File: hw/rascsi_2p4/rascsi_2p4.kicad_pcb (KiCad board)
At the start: 2 copper layers, 65 x 56 mm, 71 parts, among them J1 Raspberry_Pi_2_3, J10 Conn_01x04_Male, J2 DNP, J20 171826-4, J3 Conn_02x25_Odd_Even, J4 I2C Pinout, J5 DNP, J6 CONNFLY DB-25, J7 DNP, J8 USB_B_Micro, J9 Conn_02x25_Odd_Even, U1 SN74LS641-1DW, U2 SN74LS641-1DW, U3 SN74LS641-1DW, U4 SN74LS641-1DW, U5 UCC5606PWPTR, U6 UCC5606PWPTR, X1 Mac, X3 Mac, X7 Pi, X8 Pi

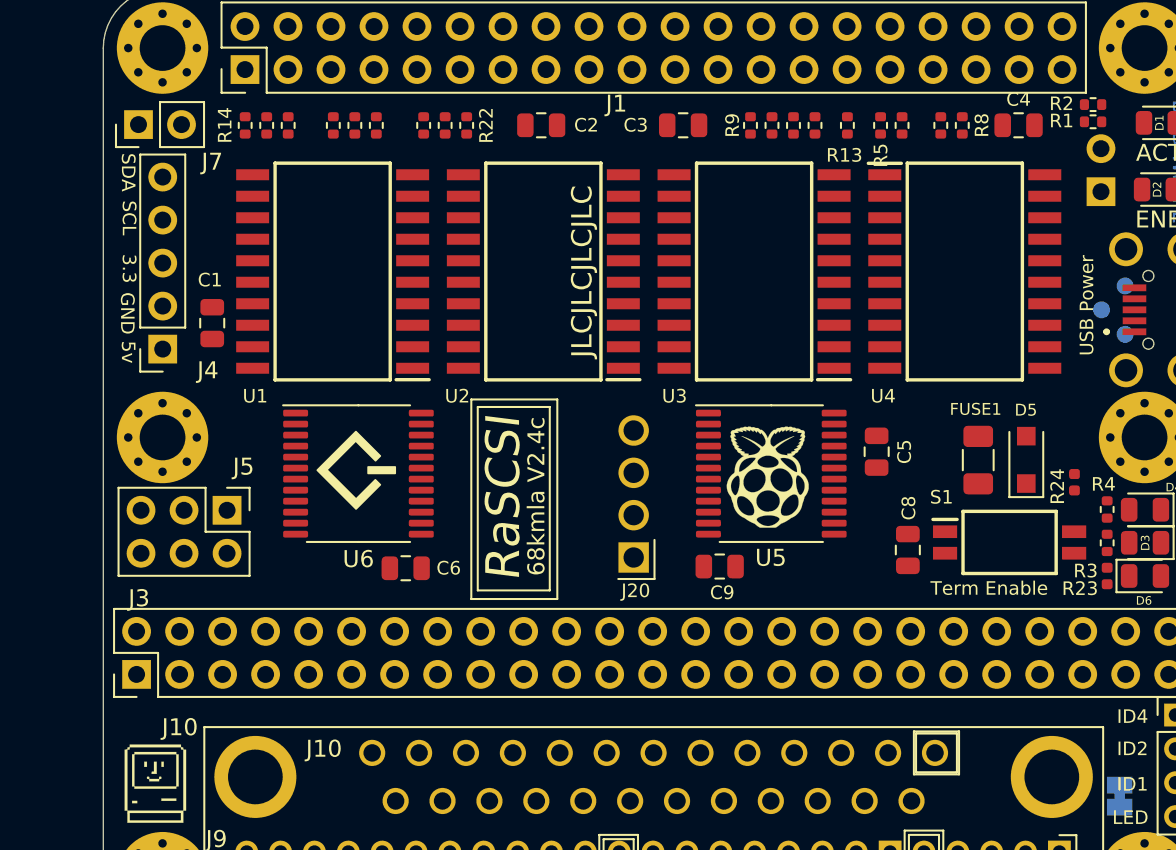
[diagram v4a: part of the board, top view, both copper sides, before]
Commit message: routed with 99 vias but not imported
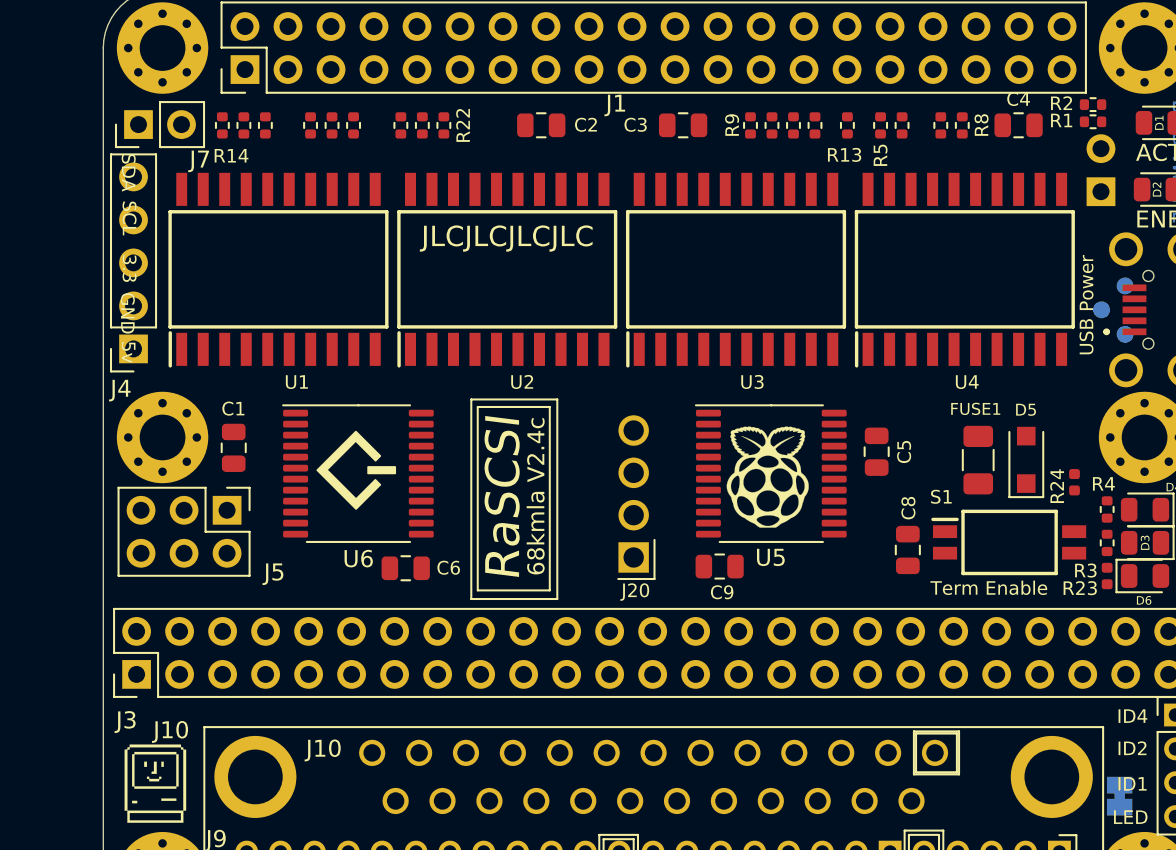
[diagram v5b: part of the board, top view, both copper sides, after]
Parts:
- moved C1 7.47 mm to (182.2, 69.6), turned to 270 degrees
- moved U1 3.20 mm to (184.8, 59.1), turned to 90 degrees
- moved U2 2.14 mm to (198.4, 59.1), turned to 90 degrees
- moved J4 1.72 mm to (176.3, 63.8)
- moved R15 1.35 mm to (182.8, 50.6)
- moved R18 1.35 mm to (188.0, 50.6)
- moved R19 1.35 mm to (189.3, 50.6)
- moved R21 1.35 mm to (193.3, 50.6)
- moved R22 1.35 mm to (194.6, 50.6)
- moved R14 1.35 mm to (181.5, 50.6)
- moved R16 1.35 mm to (184.1, 50.6)
- moved R17 1.35 mm to (186.7, 50.6)
- moved R20 1.35 mm to (192.1, 50.6)
- moved U3 1.07 mm to (211.9, 59.1), turned to 90 degrees
- moved U4 0.13 mm to (225.4, 59.1), turned to 90 degrees
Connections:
- U6 pad 1: C-D7 -> C-D5
- U6 pad 3: C-D5 -> C-D7

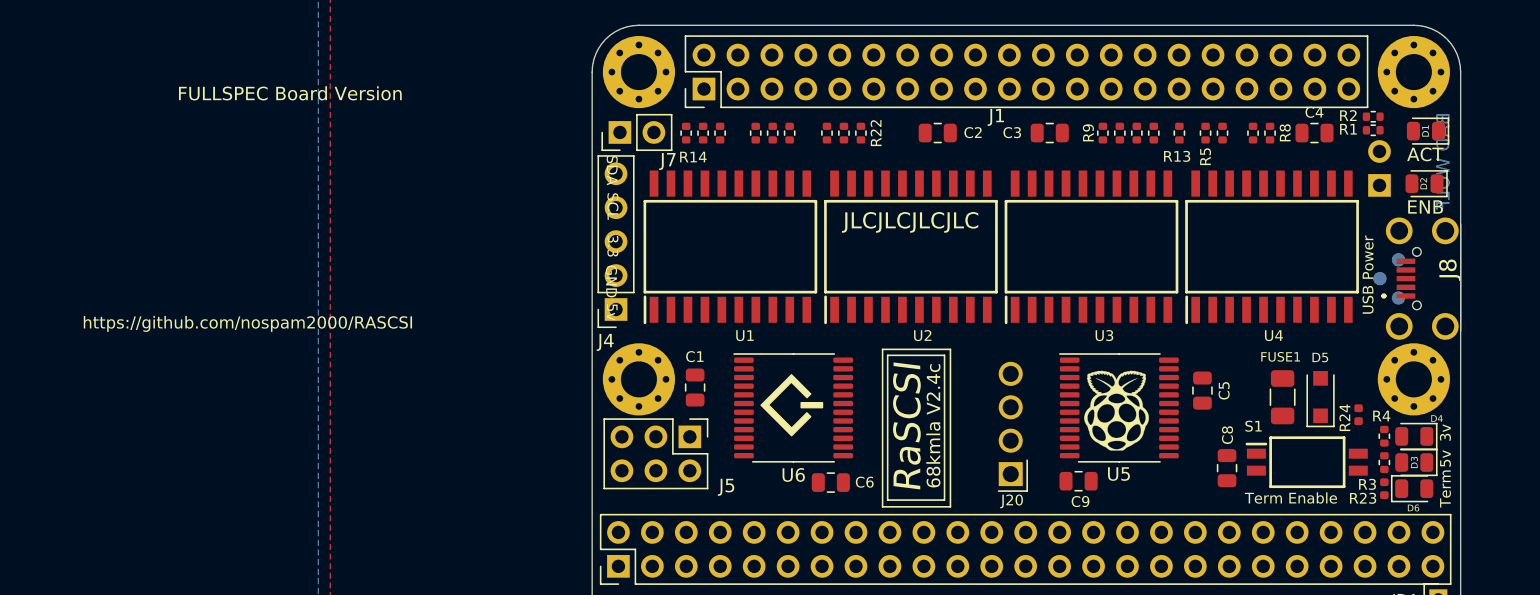
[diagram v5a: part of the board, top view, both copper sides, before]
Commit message: moved components to make space for 50 pin conn
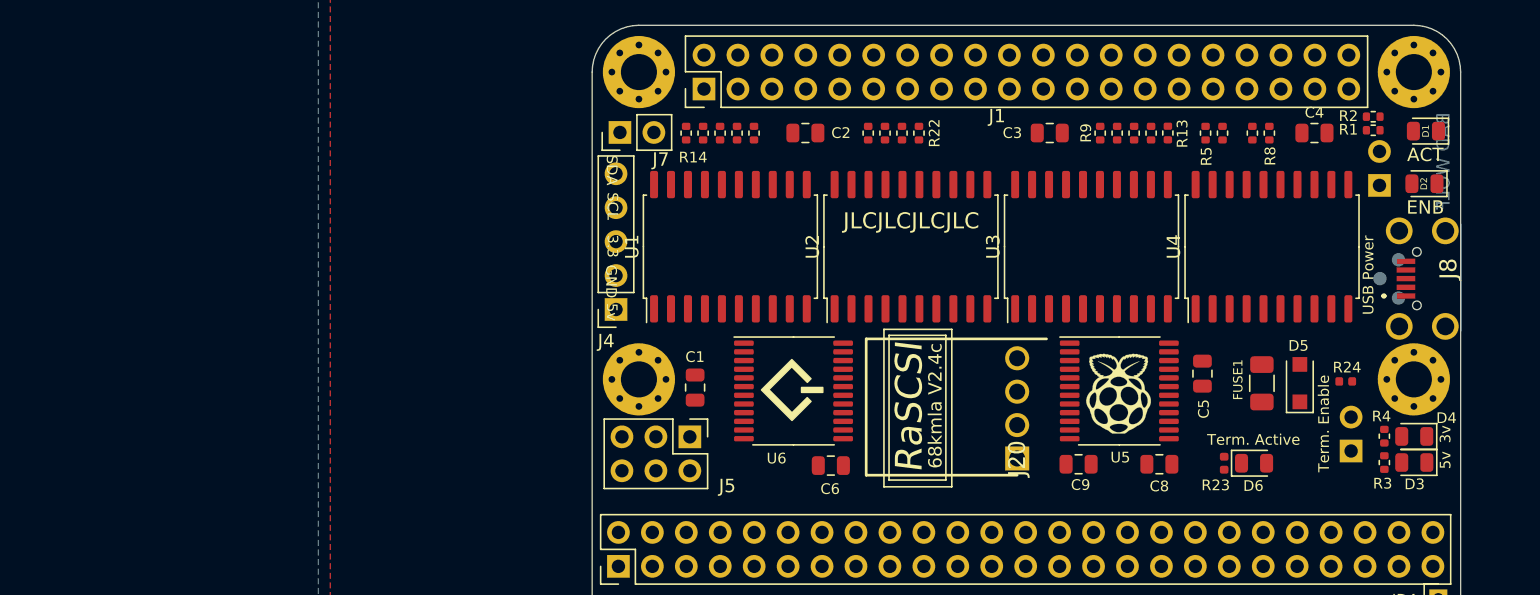
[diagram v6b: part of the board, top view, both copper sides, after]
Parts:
- removed S1: Switch x2, rascsi_din:SOIC127P812X230-4N
- added JP2: Jumper_2_Open, Connector_PinHeader_2.54mm:PinHeader_1x02_P2.54mm_Horizontal, B.Cu at (231.3, 74.4)
- U1, U2, U3, U4: footprint SamacSys_Parts:SOIC127P1030X265-20N -> Package_SO:SOIC-20W_7.5x12.8mm_P1.27mm
- moved D6 12.1 mm to (224.0, 75.3)
- moved R23 12.1 mm to (221.8, 75.3)
- moved C2 9.91 mm to (190.5, 50.6)
- moved R19 5.88 mm to (195.2, 50.6)
- moved C8 5.08 mm to (217.0, 75.4), turned to 180 degrees
- moved R20 4.34 mm to (196.4, 50.6)
- moved R21 4.34 mm to (197.7, 50.6)
- moved R22 4.34 mm to (199.0, 50.6)
- moved R24 2.67 mm to (230.9, 69.2), turned to 180 degrees
- moved FUSE1 1.87 mm to (224.6, 69.3)
- moved D5 1.87 mm to (227.5, 69.3)
- moved R17 1.40 mm to (185.3, 50.6)
- moved R18 1.40 mm to (186.6, 50.6)
- moved X7 1.28 mm to (213.9, 70.1)
- moved C6 1.27 mm to (192.4, 75.5)
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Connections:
- C1 pad 1: +5V -> PULLUP1
- C2 pad 1: +5V -> PULLUP1
- C3 pad 1: +5V -> PULLUP1
- C4 pad 1: +5V -> PULLUP1
- C8 pad 1: +5V -> PULLUP1
- D5 pad 2: +5V -> PULLUP1
- J1 pad 2: +5V -> PULLUP1
- J1 pad 4: +5V -> PULLUP1
- J20 pad 1: +5V -> PULLUP1
- J4 pad 1: +5V -> PULLUP1
- J7 pad 1: +5V -> PULLUP1
- J8 pad 1: +5V -> PULLUP1
- J9 pad 11: +5V -> PULLUP1
- J9 pad 12: +5V -> PULLUP1
- J9 pad 49: +5V -> PULLUP1
- J9 pad 50: +5V -> PULLUP1
- R23 pad 1: +5V -> PULLUP1
- R24 pad 2: +5V -> PULLUP1
- R3 pad 1: +5V -> PULLUP1
- U1 pad 11: PI-D0 -> PULLUP1
- U1 pad 12: PI-D1 -> PULLUP1
- U1 pad 13: PI-D2 -> PULLUP1
- U1 pad 20: +5V -> PULLUP1
- U1 pad 7: C-D2 -> PULLUP1
- U1 pad 8: C-D1 -> PULLUP1
- U1 pad 9: C-D0 -> PULLUP1
- U2 pad 11: GND -> PULLUP1
- U2 pad 12: GND -> PULLUP1
- U2 pad 13: GND -> PULLUP1
- U2 pad 14: GND -> PULLUP1
- U2 pad 15: GND -> PI-DP
- U2 pad 16: GND -> PI-D0
- U2 pad 17: GND -> PI-D1
- U2 pad 18: PI-DP -> PI-D2
- U2 pad 2: C-DP -> C-D2
- U2 pad 20: +5V -> PULLUP1
- U2 pad 3: GND -> C-D1
- U2 pad 4: GND -> C-D0
- U2 pad 5: GND -> C-DP
- U2 pad 6: GND -> PULLUP1
- U2 pad 7: GND -> PULLUP1
- U2 pad 8: GND -> PULLUP1
- U2 pad 9: GND -> PULLUP1
- U3 pad 16: GND -> PULLUP1
- U3 pad 17: GND -> PULLUP1
- U3 pad 18: GND -> PULLUP1
- U3 pad 2: GND -> PULLUP1
- U3 pad 20: +5V -> PULLUP1
- U3 pad 3: GND -> PULLUP1
- U3 pad 4: GND -> PULLUP1
- U4 pad 11: GND -> PULLUP1
- U4 pad 12: GND -> PULLUP1
- U4 pad 13: GND -> PULLUP1
- U4 pad 14: GND -> PULLUP1
- U4 pad 20: +5V -> PULLUP1
- U4 pad 6: GND -> PULLUP1
- U4 pad 7: GND -> PULLUP1
- U4 pad 8: GND -> PULLUP1
- U4 pad 9: GND -> PULLUP1
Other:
- net class Power: trace_width 0.6 -> 0.5; via_dia 1 -> 0.9
- net class PowerLight added: clearance 0.127, trace_width 0.4, via_dia 0.9, via_drill 0.6
- board text added: "FULLSPEC Board Version with active termination"
- board text added: "Term. Active"
- board text added: "Term. Enable"
- board text removed: "FULLSPEC Board Version"
- board text removed: "Term"
- board text removed: "Term Enable"

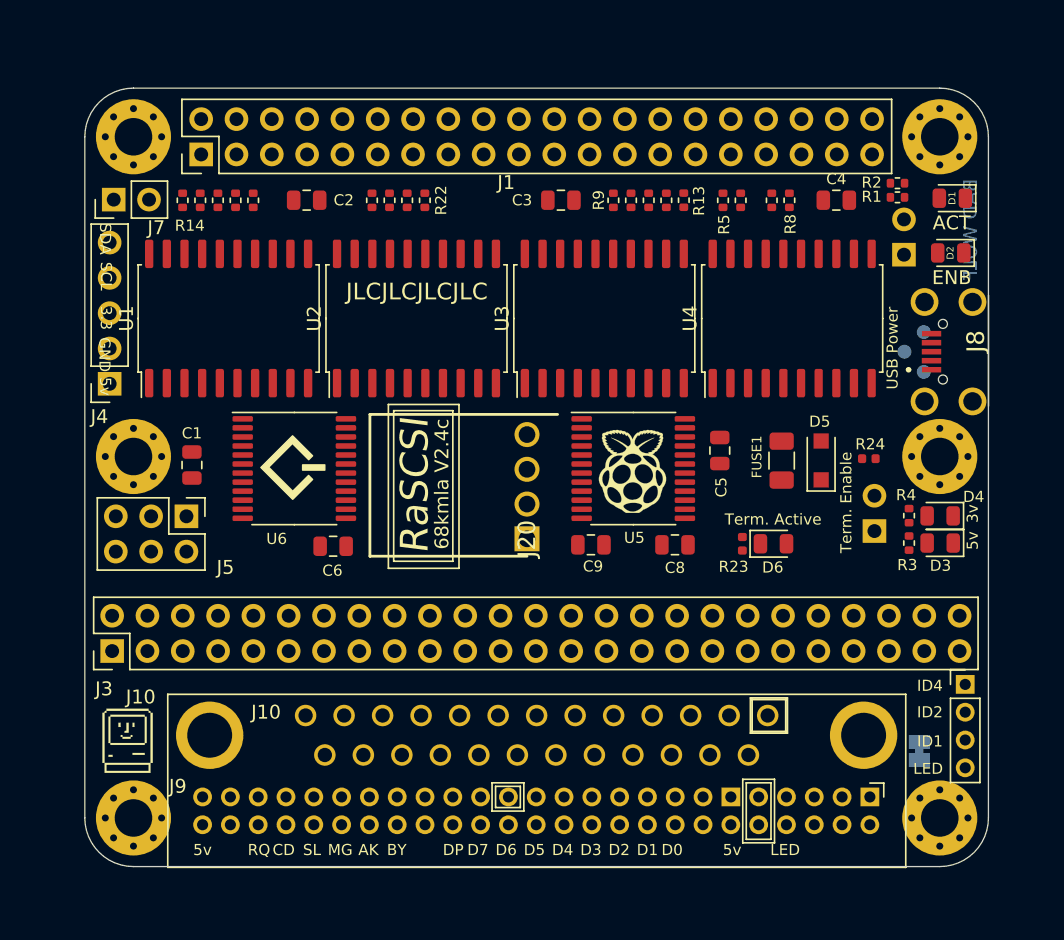
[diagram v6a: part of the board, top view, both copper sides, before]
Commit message: optimized routing (81 vias)
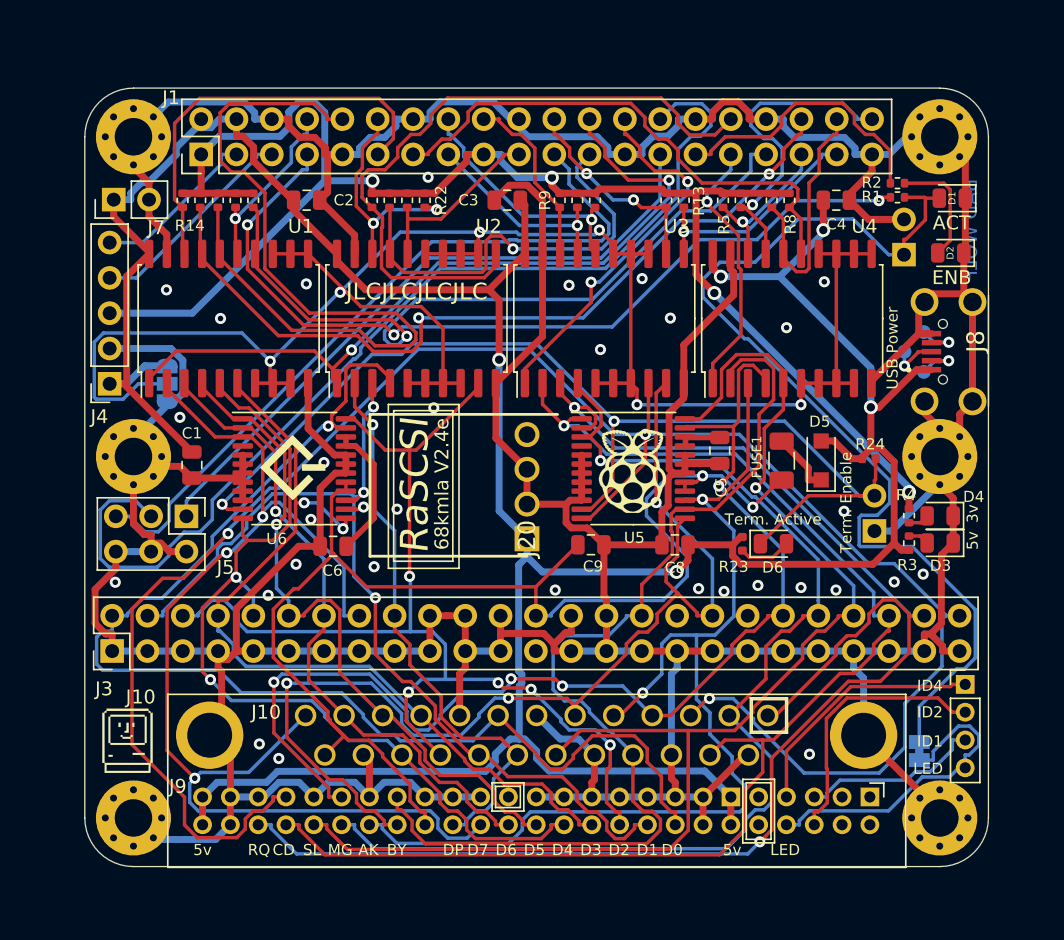
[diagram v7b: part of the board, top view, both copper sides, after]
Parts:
- added JP3: PULLUP Power, Jumper:SolderJumper-3_P1.3mm_Bridged12_RoundedPad1.0x1.5mm, B.Cu at (180.4, 63.8)
- R23: value 2k -> 5.1k
- moved C3 3.86 mm to (204.9, 50.6)
- moved R11 3.86 mm to (211.2, 50.6)
- moved R9 3.86 mm to (208.7, 50.6)
- moved R10 3.86 mm to (209.9, 50.6)
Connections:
- C1 pad 1: PULLUP1 -> +5V
- C2 pad 1: PULLUP1 -> +5V
- C3 pad 1: PULLUP1 -> +5V
- C4 pad 1: PULLUP1 -> +5V
- C8 pad 1: PULLUP1 -> +5V
- D5 pad 2: PULLUP1 -> +5V
- J1 pad 2: PULLUP1 -> +5V
- J1 pad 4: PULLUP1 -> +5V
- J20 pad 1: PULLUP1 -> +5V
- J4 pad 1: PULLUP1 -> +5V
- J7 pad 1: PULLUP1 -> +5V
- J8 pad 1: PULLUP1 -> +5V
- J9 pad 11: PULLUP1 -> +5V
- J9 pad 12: PULLUP1 -> +5V
- J9 pad 49: PULLUP1 -> +5V
- J9 pad 50: PULLUP1 -> +5V
- R10 pad 2: PI-MSG -> PI-REQ
- R11 pad 2: PI-C_D -> PI-MSG
- R12 pad 2: PI-REQ -> PI-I_O
- R13 pad 2: PI-I_O -> PI-BSY
- R23 pad 1: PULLUP1 -> +5V
- R24 pad 2: PULLUP1 -> +5V
- R3 pad 1: PULLUP1 -> +5V
- R9 pad 2: PI-BSY -> PI-C_D
- U1 pad 11: PULLUP1 -> PULLUP_OC
- U1 pad 12: PULLUP1 -> PULLUP_OC
- U1 pad 13: PULLUP1 -> PULLUP_OC
- U1 pad 20: PULLUP1 -> +5V
- U1 pad 7: PULLUP1 -> PULLUP_OC
- U1 pad 8: PULLUP1 -> PULLUP_OC
- U1 pad 9: PULLUP1 -> PULLUP_OC
- U2 pad 11: PULLUP1 -> PI-D2
- U2 pad 12: PULLUP1 -> PULLUP_OC
- U2 pad 13: PULLUP1 -> PULLUP_OC
- U2 pad 14: PULLUP1 -> PULLUP_OC
- U2 pad 15: PI-DP -> PULLUP_OC
- U2 pad 18: PI-D2 -> PI-DP
- U2 pad 2: C-D2 -> C-DP
- U2 pad 20: PULLUP1 -> +5V
- U2 pad 5: C-DP -> PULLUP_OC
- U2 pad 6: PULLUP1 -> PULLUP_OC
- U2 pad 7: PULLUP1 -> PULLUP_OC
- U2 pad 8: PULLUP1 -> PULLUP_OC
- U2 pad 9: PULLUP1 -> C-D2
- U3 pad 11: PI-I_O -> PI-BSY
- U3 pad 12: PI-REQ -> PI-I_O
- U3 pad 13: PI-C_D -> PULLUP_OC
- U3 pad 14: PI-MSG -> PULLUP_OC
- U3 pad 15: PI-BSY -> PULLUP_OC
- U3 pad 16: PULLUP1 -> PI-MSG
- U3 pad 17: PULLUP1 -> PI-REQ
- U3 pad 18: PULLUP1 -> PI-C_D
- U3 pad 2: PULLUP1 -> C-C_D
- U3 pad 20: PULLUP1 -> +5V
- U3 pad 3: PULLUP1 -> C-REQ
- U3 pad 4: PULLUP1 -> C-MSG
- U3 pad 5: C-BSY -> PULLUP_OC
- U3 pad 6: C-MSG -> PULLUP_OC
- U3 pad 7: C-C_D -> PULLUP_OC
- U3 pad 8: C-REQ -> C-I_O
- U3 pad 9: C-I_O -> C-BSY
- U4 pad 11: PULLUP1 -> PULLUP_OC
- U4 pad 12: PULLUP1 -> PULLUP_OC
- U4 pad 13: PULLUP1 -> PULLUP_OC
- U4 pad 14: PULLUP1 -> PULLUP_OC
- U4 pad 20: PULLUP1 -> +5V
- U4 pad 6: PULLUP1 -> PULLUP_OC
- U4 pad 7: PULLUP1 -> PULLUP_OC
- U4 pad 8: PULLUP1 -> PULLUP_OC
- U4 pad 9: PULLUP1 -> PULLUP_OC
- U5 pad 1: C-BSY -> C-C_D
- U5 pad 12: C-REQ -> C-I_O
- U5 pad 13: C-I_O -> C-BSY
- U5 pad 2: C-MSG -> C-REQ
- U5 pad 3: C-C_D -> C-MSG
- U6 pad 14: C-D2 -> C-DP
- U6 pad 24: C-DP -> C-D2
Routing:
- net GND: track 0.00 -> 542.9 mm, vias 0 -> 31
- net +5V: track 0.00 -> 231.1 mm, vias 0 -> 5
- net C-I_O: track 0.00 -> 143.8 mm, vias 0 -> 3
- net PULLUP_OC: track 0.00 -> 131.8 mm, vias 0 -> 6
- net C-REQ: track 0.00 -> 112.6 mm, vias 0 -> 2
- net +3V3: track 0.00 -> 110.7 mm, vias 0 -> 4
- net C-C_D: track 0.00 -> 95.1 mm, vias 0 -> 1
- net C-SEL: track 0.00 -> 94.0 mm, vias 0 -> 1
- net TERMPOW: track 0.00 -> 90.1 mm, vias 0 -> 2
- net C-D0: track 0.00 -> 88.4 mm, vias 0 -> 1
- net C-D7: track 0.00 -> 84.3 mm, vias 0 -> 3
- net C-RST: track 0.00 -> 82.7 mm, vias 0 -> 4
- net C-MSG: track 0.00 -> 82.1 mm, vias 0 -> 1
- net C-BSY: track 0.00 -> 79.7 mm, vias 0 -> 3
- net C-D2: track 0.00 -> 78.3 mm, vias 0 -> 5
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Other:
- board text added: "68kmla V2.4e"
- board text added: "68kmla Version 2.4e"
- board text removed: "68kmla V2.4c"
- board text removed: "68kmla Version 2.4c"

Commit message: changed sild label "Term." by "Termination"
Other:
- board text added: "Termination Enable"
